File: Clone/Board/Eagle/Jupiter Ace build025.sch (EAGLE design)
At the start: 325 parts, among them K1 1, K10 0, K11 Q, K12 W, K13 E, K14 R, K15 T, K16 Y, K17 U, K18 I, K19 O, K2 2, K20 P, K21 A, K22 S, K23 D, K24 F, K25 G, K26 H, K27 J, K28 K, K29 L, K3 3, K30 ENTER, K31 SHIFT, K32 SYMBOL, K33 Z, K34 X, K35 C, K36 V, K37 B, K38 N, K39 M, K4 4, K40 SPACE, K41 SPACE, K5 5, K6 6, K7 7, K8 8, K9 9, Q1 2N3904, Q3 BC337, U1 7805, U2 MAX4390EUK, X1 6.5MHz, X2 CON-CONRAD_736880-49

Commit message: build 25
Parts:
- added C23: 10pF, rcl:C-EU025-025X050
- added JP11, JP12: (no value), pinhead:PINHD-2X5
- added JP14: (no value), pinhead:PINHD-1X1
- added JP16: (no value), pinhead:PINHD-2X8
- added JP17, JP18: (no value), pinhead:PINHD-1X2
- added JP2, JP9: (no value), pinhead:PINHD-1X20
- added R44: 1K, pot:TRIM_EU-B25P
- R21, R22, R23: device rcl:R-EU_0204/7 -> rcl:R-EU_0204/2V
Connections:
- net N$52 renamed CNT3'
- net N$53 renamed CNT14'
- net N$54 renamed CNT13'
- net N$55 renamed CNT12'
- net N$79 renamed CNT7'
- net N$87 renamed CNT6'
- net N$88 renamed CNT5'
- net N$89 renamed CNT4'
- net N$90 renamed CNT15'
- net N$92 renamed CNT16'
- new net N$33: C23.2, R44.A, Z28A.CLK
- new net N$57: JP11.8, Z5-6G$1.A13
- new net N$62: JP11.4, Z5-6G$1.A11
- new net N$66: JP11.2, Z5-6G$1.A10
- new net N$67: JP11.6, Z5-6G$1.A12
- new net N$68: JP11.10, Z5-6G$1.A14
- new net N$69: JP12.8, Z7-8G$1.A13
- new net N$71: JP12.2, Z7-8G$1.A10
- new net N$82: JP12.4, Z7-8G$1.A11
- new net N$84: JP12.6, Z7-8G$1.A12
- new net N$85: JP12.10, Z7-8G$1.A14
- new net N$91: JP17.1, R23.1
- net /BUSAK: now also JP9.18
- net /BUSRQ: now also JP9.16
- net /HALT: now also JP2.18
- net /INT: now also JP2.16
- net /IORQ: now also JP2.20
- net /M1: now also JP9.14
- net /MREQ: now also JP2.19
- net /NMI: now also JP2.17
- net /RD: now also JP9.20
- net /RFSH: now also JP9.13
- net /WAIT: now also JP9.17
- net /WR: now also JP9.19
- net A0: now also JP9.11
- net A1: now also JP9.10
- net A10: now also JP9.1
- net A11: now also JP2.1
- net A12: now also JP2.2
- net A13: now also JP2.3
- net A14: now also JP2.4
- net A15: now also JP2.5
- net A2: now also JP9.9
- net A3: now also JP9.8
- net A4: now also JP9.7
- net A5: now also JP9.6
- net A6: now also JP9.5
- net A7: now also JP9.4
- net A8: now also JP9.3
- net A9: now also JP9.2
- net CLK: now also R44.E, R44.S; no longer Z28A.CLK
- net CNT10: now also JP18.1
- net CNT11: now also JP17.2; no longer R23.1
- net CNT9: now also JP18.2
- net D0: now also JP2.14
- net D1: now also JP2.15
- net D2: now also JP2.12
- net D3: now also JP2.8
- net D4: now also JP2.7
- net D5: now also JP2.9
- net D6: now also JP2.10
- net D7: now also JP2.13
- net GND: now also C23.1, JP11.1, JP11.3, JP11.5, JP11.7, JP11.9, JP12.1, JP12.3, JP12.5, JP12.7, JP12.9, JP9.12; no longer Z5-6G$1.A10, Z5-6G$1.A11, Z5-6G$1.A12, Z5-6G$1.A13, Z5-6G$1.A14, Z7-8G$1.A10, Z7-8G$1.A11, Z7-8G$1.A12, Z7-8G$1.A13, Z7-8G$1.A14
- net KB: now also JP16.12, JP16.5
- net KC: now also JP16.7
- net KEYB2: now also JP16.2, SJ2.2
- net KEYB3: now also JP16.4, SJ3.2
- net KEYB4: now also JP16.6, SJ4.2
- net KEYB5: now also JP16.8, SJ5.2
- net KM: now also JP16.1
- net KN: now also JP16.3, JP16.9
- net KX: now also JP16.11
- net KZ: now also JP16.10
- net N$101: no longer SJ8.2
- net N$112: no longer SJ5.2
- net N$32: no longer SJ9.2
- net N$46: no longer SJ4.2
- net N$50: no longer SJ2.2
- net N$51: no longer SJ3.2
- net N$59: now also JP14.1
- net PHI: now also JP2.6
- net RESET: now also JP9.15
- net ROW1: now also JP16.13
- net ROW8: now also JP16.15
- net ROW_SS: now also JP16.14, SJ8.2
- net ROW_V: now also JP16.16, SJ9.2
- net VCC: now also JP2.11
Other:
- moved on the sheet: Z7-8

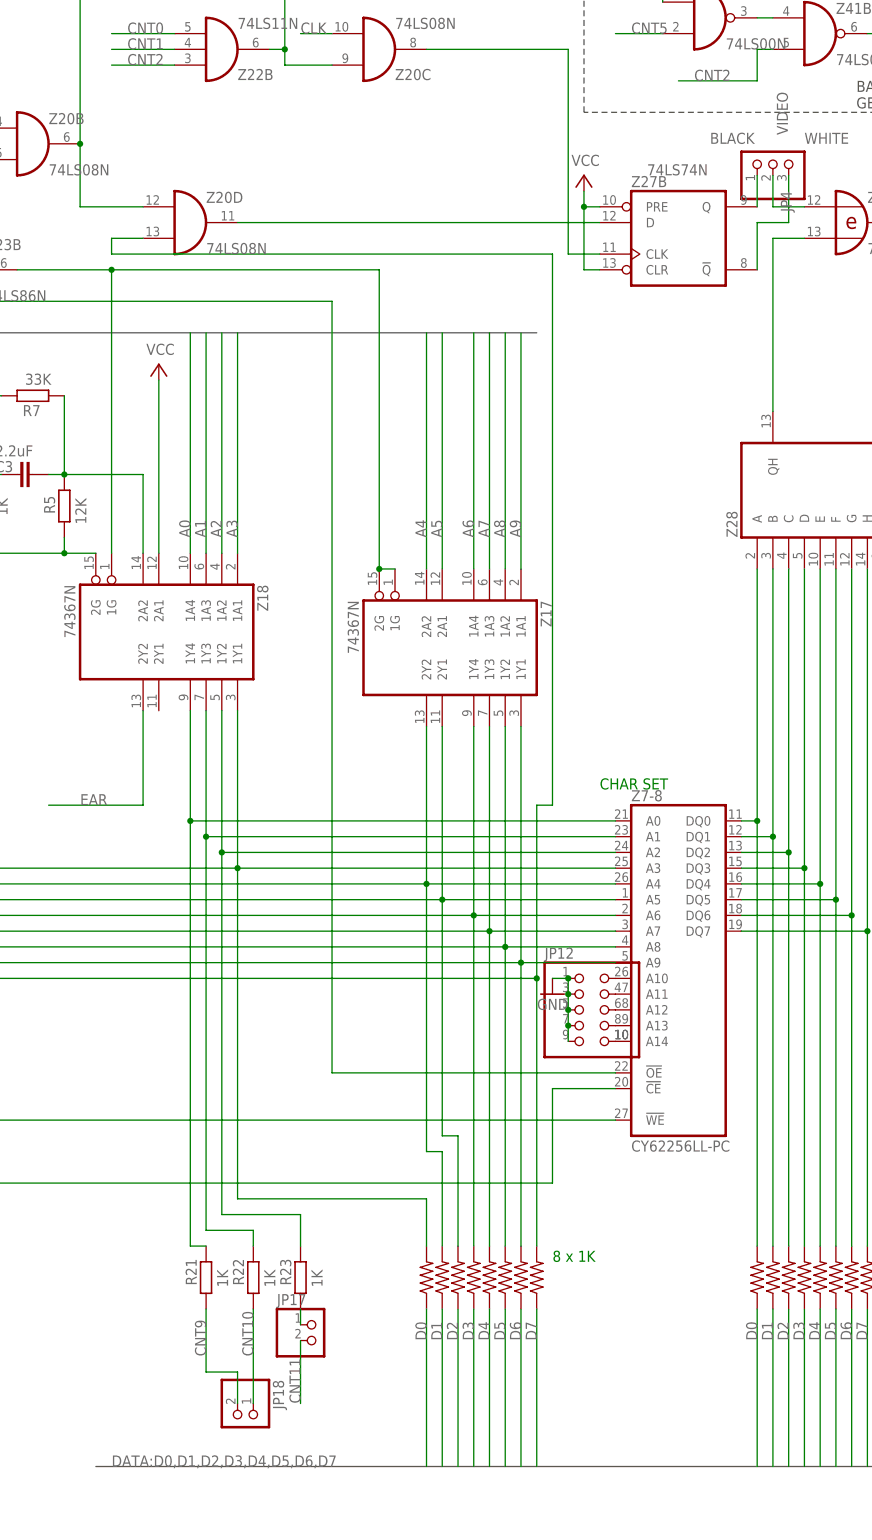
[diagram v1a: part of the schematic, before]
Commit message: capture inv bit
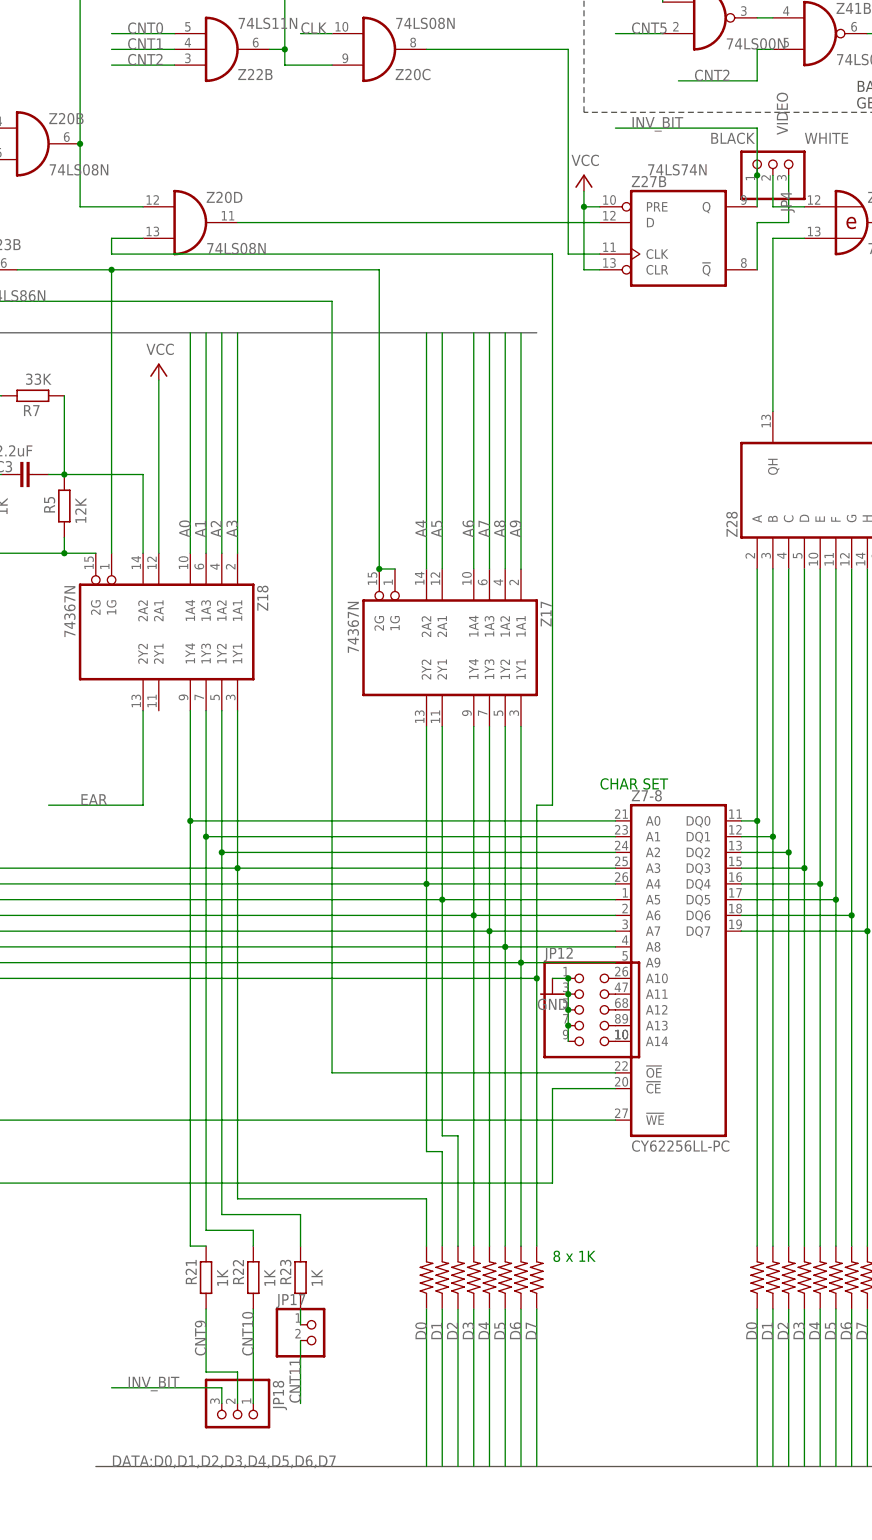
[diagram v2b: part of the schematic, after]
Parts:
- JP18: device pinhead:PINHD-1X2 -> pinhead:PINHD-1X3
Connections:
- removed net N$15: JP4.1, Z27B.Q
- new net INV_BIT: JP18.3, JP4.1, Z27B.Q
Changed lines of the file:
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@@
 <part name="JP16" library="pinhead" library_urn="urn:adsk.eagle:library:44166543" deviceset="PINHD-2X8" device="" package3d_urn="urn:adsk.eagle:package:22481/2"/>
 <part name="JP17" library="pinhead" library_urn="urn:adsk.eagle:library:44166543" deviceset="PINHD-1X2" device="" package3d_urn="urn:adsk.eagle:package:22435/2"/>
-<part name="JP18" library="pinhead" library_urn="urn:adsk.eagle:library:44166543" deviceset="PINHD-1X2" device="" package3d_urn="urn:adsk.eagle:package:22435/2"/>
+<part name="JP18" library="pinhead" library_urn="urn:adsk.eagle:library:44166543" deviceset="PINHD-1X3" device="" package3d_urn="urn:adsk.eagle:package:22458/2"/>
 </parts>
 <sheets>
@@
 <attribute name="VALUE" x="549.91" y="-119.38" size="1.778" layer="96"/>
 </instance>
-<instance part="JP18" gate="G$1" x="543.56" y="-127" smashed="yes" rot="R270">
+<instance part="JP18" gate="A" x="543.56" y="-127" smashed="yes" rot="R270">
 <attribute name="NAME" x="549.275" y="-120.65" size="1.778" layer="95" rot="R270"/>
-<attribute name="VALUE" x="538.48" y="-120.65" size="1.778" layer="96" rot="R270"/>
+<attribute name="VALUE" x="535.94" y="-120.65" size="1.778" layer="96" rot="R270"/>
 </instance>
 </instances>
@@
 <wire x1="538.48" y1="-119.38" x2="543.56" y2="-119.38" width="0.1524" layer="91"/>
 <wire x1="543.56" y1="-119.38" x2="543.56" y2="-124.46" width="0.1524" layer="91"/>
-<pinref part="JP18" gate="G$1" pin="2"/>
+<pinref part="JP18" gate="A" pin="2"/>
 </segment>
 <segment>
@@
 <label x="546.1" y="-116.84" size="1.778" layer="95" rot="R90"/>
 <wire x1="546.1" y1="-109.22" x2="546.1" y2="-124.46" width="0.1524" layer="91"/>
-<pinref part="JP18" gate="G$1" pin="1"/>
+<pinref part="JP18" gate="A" pin="1"/>
 </segment>
 <segment>
@@
 </segment>
 </net>
-<net name="N$15" class="0">
+<net name="INV_BIT" class="0">
 <segment>
 <pinref part="Z27" gate="B" pin="Q"/>
 <pinref part="JP4" gate="A" pin="1"/>
 <wire x1="627.38" y1="68.58" x2="627.38" y2="73.66" width="0.1524" layer="91"/>
+<wire x1="627.38" y1="73.66" x2="627.38" y2="81.28" width="0.1524" layer="91"/>
+<junction x="627.38" y="73.66"/>
+<wire x1="627.38" y1="81.28" x2="604.52" y2="81.28" width="0.1524" layer="91"/>
+<label x="607.06" y="81.28" size="1.778" layer="95"/>
+</segment>
+<segment>
+<pinref part="JP18" gate="A" pin="3"/>
+<wire x1="541.02" y1="-124.46" x2="541.02" y2="-121.92" width="0.1524" layer="91"/>
+<wire x1="541.02" y1="-121.92" x2="523.24" y2="-121.92" width="0.1524" layer="91"/>
+<label x="525.78" y="-121.92" size="1.778" layer="95"/>
 </segment>
 </net>
